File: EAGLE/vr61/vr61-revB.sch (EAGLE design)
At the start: 186 parts, among them M1 M25C, X1 MICROMOD-2222-C

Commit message: minor edits
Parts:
- added S3: BOOT, SparkFun-Switches:MOMENTARY-SWITCH-SPST-SMD-5.2-TALL-REDUNDANT
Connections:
- net !BOOT: now also S3.2
- net GND: now also S3.1
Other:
- note added: "Do not populate"
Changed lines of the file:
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@@
 <part name="J-52" library="SparkFun-Connectors" library_urn="urn:adsk.eagle:library:513" deviceset="CONN_03" device="" package3d_urn="urn:adsk.eagle:package:38063/1"/>
 <part name="U$14" library="ts_keyboards" deviceset="74AHCT1G125GW" device=""/>
+<part name="S3" library="SparkFun-Switches" deviceset="MOMENTARY-SWITCH-SPST" device="-SMD-5.2-TALL-REDUNDANT" value="BOOT"/>
 </parts>
 <sheets>
@@
 <text x="48.26" y="58.42" size="1.778" layer="91">SPI EEPROM</text>
 <text x="180.34" y="55.88" size="1.778" layer="91">TE P# 2199119-4</text>
+<text x="269.24" y="157.48" size="1.778" layer="91" rot="R90">Do not populate</text>
+<text x="67.818" y="37.084" size="1.778" layer="91" rot="R180">Do not populate</text>
 </plain>
 <instances>
@@
 <attribute name="NAME" x="256.54" y="162.052" size="1.778" layer="95" font="vector" rot="R180"/>
 </instance>
-<instance part="GND10" gate="1" x="243.84" y="162.56" smashed="yes">
-<attribute name="VALUE" x="243.84" y="157.988" size="1.778" layer="96" align="top-center"/>
+<instance part="GND10" gate="1" x="241.3" y="157.48" smashed="yes">
+<attribute name="VALUE" x="241.3" y="152.908" size="1.778" layer="96" align="top-center"/>
 </instance>
 <instance part="U$4" gate="G$1" x="248.92" y="63.5" smashed="yes">
@@
 <attribute name="NAME" x="147.32" y="21.59" size="1.27" layer="95"/>
 <attribute name="VALUE" x="143.256" y="8.128" size="1.27" layer="96"/>
+</instance>
+<instance part="S3" gate="G$1" x="264.16" y="165.1" smashed="yes" rot="R90">
+<attribute name="NAME" x="262.636" y="165.1" size="1.778" layer="95" font="vector" rot="R90" align="bottom-center"/>
+<attribute name="VALUE" x="264.668" y="165.1" size="1.778" layer="96" font="vector" rot="R90" align="top-center"/>
 </instance>
 </instances>
@@
 <wire x1="246.38" y1="165.1" x2="243.84" y2="165.1" width="0.1524" layer="91"/>
 <pinref part="GND10" gate="1" pin="GND"/>
-<wire x1="243.84" y1="165.1" x2="243.84" y2="162.56" width="0.1524" layer="91"/>
+<wire x1="243.84" y1="165.1" x2="241.3" y2="165.1" width="0.1524" layer="91"/>
+<wire x1="241.3" y1="165.1" x2="241.3" y2="157.48" width="0.1524" layer="91"/>
+<pinref part="S3" gate="G$1" pin="1"/>
+<wire x1="264.16" y1="160.02" x2="264.16" y2="157.48" width="0.1524" layer="91"/>
+<wire x1="264.16" y1="157.48" x2="246.38" y2="157.48" width="0.1524" layer="91"/>
+<wire x1="246.38" y1="157.48" x2="246.38" y2="160.02" width="0.1524" layer="91"/>
+<wire x1="246.38" y1="160.02" x2="243.84" y2="160.02" width="0.1524" layer="91"/>
+<wire x1="243.84" y1="160.02" x2="243.84" y2="165.1" width="0.1524" layer="91"/>
+<junction x="243.84" y="165.1"/>
 </segment>
 <segment>
@@
 <pinref part="J-BOOT" gate="G$1" pin="1"/>
 <wire x1="246.38" y1="167.64" x2="243.84" y2="167.64" width="0.1524" layer="91"/>
-<label x="243.84" y="167.64" size="1.778" layer="95" rot="R180" xref="yes"/>
-</segment>
-</net>
+<label x="241.3" y="167.64" size="1.778" layer="95" rot="R180" xref="yes"/>
+<wire x1="243.84" y1="167.64" x2="241.3" y2="167.64" width="0.1524" layer="91"/>
+<wire x1="243.84" y1="167.64" x2="243.84" y2="172.72" width="0.1524" layer="91"/>
+<junction x="243.84" y="167.64"/>
+<wire x1="243.84" y1="172.72" x2="264.16" y2="172.72" width="0.1524" layer="91"/>
+<pinref part="S3" gate="G$1" pin="2"/>
+<wire x1="264.16" y1="172.72" x2="264.16" y2="170.18" width="0.1524" layer="91"/>
+</segment>
+</net>

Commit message: Reb B.2 update
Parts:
- removed JP-VIN3: OPT, SparkFun-Jumpers:JUMPER-SMT_2_NC_PASTE_NO-SILK
- added D63, D64, D65, D66, D67: (no value), jlcpcb_basic_parts:1N5819WS
- added DIP-SW: DIP004, untitled:DIP004
- added J-VIN: (no value), ts_jumpers:JUMPER-1X2
- added S_BSPC2, S_CAPS2, S_FN, S_RSFT2, S_SPARE: MX-5-PIN-MILMAX-3305-XNO-SILK, ts_keyboards:MX-5-PIN-MILMAX-3305-XNO-SILK
- added U$20, U$21, U$22: FIDUCIAL, __temp_to_delete:FIDUCIAL
- JP-GND: device SparkFun-Jumpers:JUMPER-SMT_2_NO_NO-SILK -> ts_jumpers:JUMPER-1X2
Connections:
- removed net N$68: JP-VIN3.1, R3.2
- new net N$70: D64.A, S_SPARE.P
- new net N$71: D63.A, S_FN.P
- new net N$73: D65.A, DIP-SW.1
- new net N$74: DIP-SW.4, J-VIN.2, R3.2
- new net N$75: D66.A, DIP-SW.2
- new net N$76: D67.A, DIP-SW.3
- net GROUND: now also JP-GND.2; no longer JP-GND.1
- net MX4: now also D63.C, D64.C
- net MX5: now also D65.C, D66.C, D67.C
- net MY2: now also S_CAPS2.P
- net MY5: now also DIP-SW.8, S_BSPC2.S
- net MY6: now also DIP-SW.7
- net MY7: now also DIP-SW.6, S_SPARE.S
- net MY8: now also S_FN.S, S_RSFT2.S
- net N$14: now also S_BSPC2.P
- net N$53: now also S_RSFT2.P
- net N$62: now also S_CAPS2.S
- net SC1: now also JP-GND.1; no longer JP-GND.2
- net VSUP: now also DIP-SW.5, J-VIN.1; no longer JP-VIN3.2
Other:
- note added: "<<< DNP >>> (Do Not Populate)"
- note added: "OPTIONAL Micromod Voltage Sensor & DIP Switches <<< DNP >>>"
- note removed: "Micromod Voltage Sensor"
- moved on the sheet: D01, D02, D03, D04, D05, D06, D07, D08, D09, D10, D11, D12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

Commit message: Boot switch redo
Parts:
- added C14: 100nF, rcl:C-EUC0603
- added D80: BAS70-05, diode:BAS70-05
- added R9: 5.1K, rcl:R-EU_R0603
- added S4: BOOT, SparkFun-Switches:MOMENTARY-SWITCH-SPST-SMD-5.2-TALL-REDUNDANT
- S1: value Reset -> (none); device SparkFun-Switches:MOMENTARY-SWITCH-SPST-SMD-5.2-TALL-REDUNDANT -> VinoRodrigues_Custom_Eagle:MOMENTARY-SWITCH-SPST-1
- S2: value BOOT -> (none); device SparkFun-Switches:MOMENTARY-SWITCH-SPST-SMD-5.2-TALL-REDUNDANT -> VinoRodrigues_Custom_Eagle:MOMENTARY-SWITCH-SPST-1
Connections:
- new net BOOT: D80.C, J-BOOT.1, R9.1, S3.2, S4.2
- net !BOOT: now also C14.1, D80.A1, S2.3; no longer J-BOOT.1, S2.2, S3.2
- net !RESET: now also D80.A2, S1.3; no longer S1.2
- net GND: now also C14.2, S4.1
- net VCC: now also R9.2
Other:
- note added: "<<< DNP >>> (Do Not Populate) for under space bar"
- note removed: "<<< DNP >>> (Do Not Populate)"
- moved on the sheet: S3

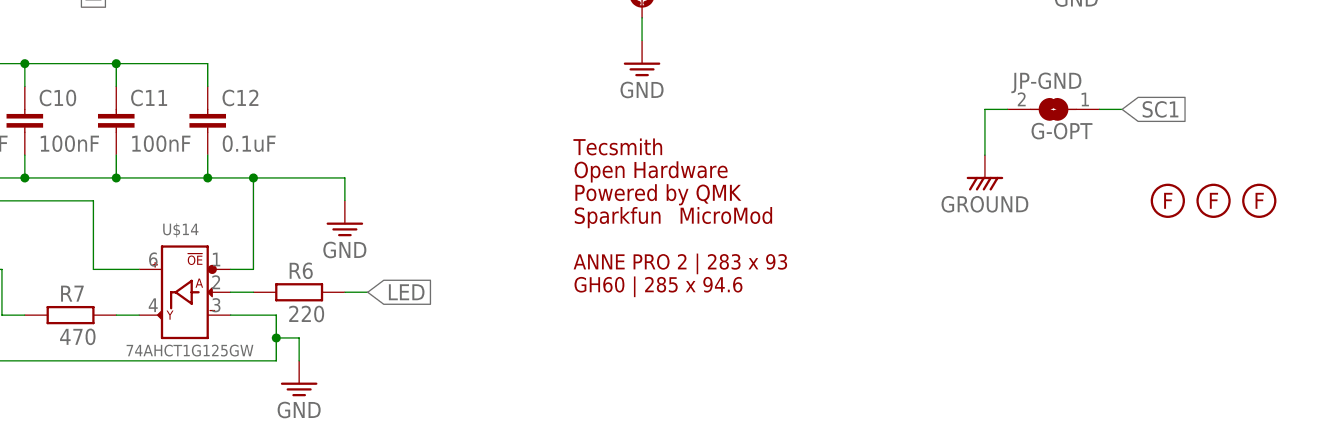
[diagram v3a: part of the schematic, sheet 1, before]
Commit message: Added Bakeneko footprint
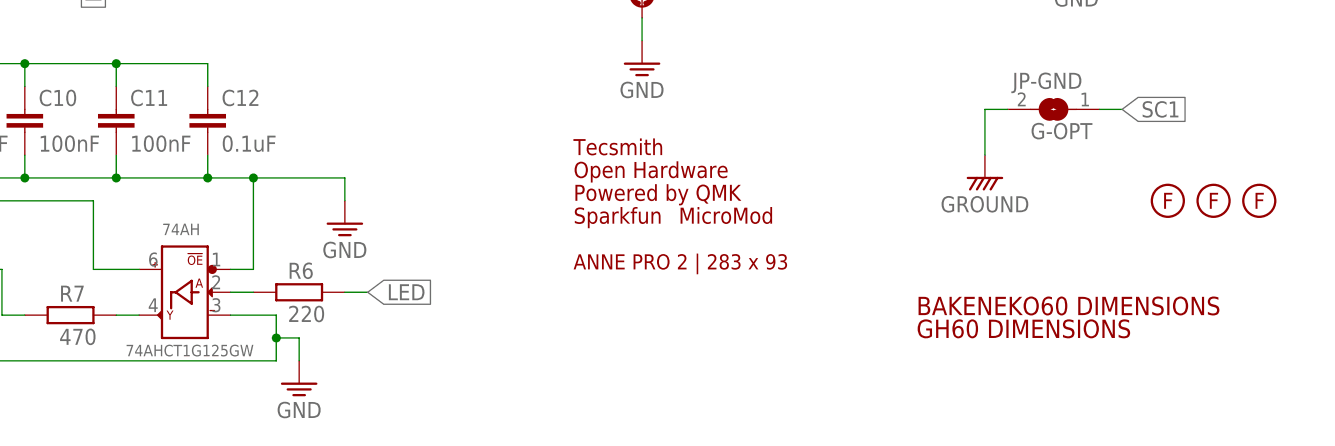
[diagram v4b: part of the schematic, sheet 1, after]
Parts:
- removed FP_GH60: FOOTPRINT-GH60, ts_keyboards:FOOTPRINT-GH60
- added U$24: FOOTPRINT-BAKENEKO60, ts_keyboards:FOOTPRINT-BAKENEKO60
- added U$25: FOOTPRINT-DIMS-GH60, ts_keyboards:FOOTPRINT-DIMS-GH60
- renumbered U$14 to 74AH
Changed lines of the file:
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@@
 <part name="GND13" library="ts_custom_nick_nacks" deviceset="GND" device=""/>
 <part name="FP_AP2" library="ts_keyboards" deviceset="FOOTPRINT-AP2" device=""/>
-<part name="FP_GH60" library="ts_keyboards" deviceset="FOOTPRINT-GH60" device=""/>
 <part name="D43" library="jlcpcb_basic_parts" deviceset="1N5819WS" device=""/>
 <part name="S_NUBS" library="ts_keyboards" deviceset="MX-5-PIN-HOTSWAP-PAD" device="NO-SILK"/>
@@
 <part name="T_ENT1" library="ts_keyboards" deviceset="MX-STABS-200U" device=""/>
 <part name="J-52" library="SparkFun-Connectors" library_urn="urn:adsk.eagle:library:513" deviceset="CONN_03" device="" package3d_urn="urn:adsk.eagle:package:38063/1"/>
-<part name="U$14" library="ts_keyboards" deviceset="74AHCT1G125GW" device=""/>
+<part name="74AH" library="ts_keyboards" deviceset="74AHCT1G125GW" device=""/>
 <part name="S4" library="SparkFun-Switches" deviceset="MOMENTARY-SWITCH-SPST" device="-SMD-5.2-TALL-REDUNDANT" value="BOOT"/>
 <part name="D63" library="jlcpcb_basic_parts" deviceset="1N5819WS" device=""/>
@@
 <part name="U$23" library="ts_custom_nick_nacks" deviceset="3V3" device=""/>
 <part name="GND14" library="ts_custom_nick_nacks" deviceset="GND" device=""/>
+<part name="U$24" library="ts_keyboards" deviceset="FOOTPRINT-BAKENEKO60" device=""/>
+<part name="U$25" library="ts_keyboards" deviceset="FOOTPRINT-DIMS-GH60" device=""/>
 </parts>
 <sheets>
@@
 </instance>
 <instance part="FP_AP2" gate="G$1" x="193.04" y="17.78" smashed="yes"/>
-<instance part="FP_GH60" gate="G$1" x="193.04" y="15.24" smashed="yes"/>
 <instance part="J-HOST" gate="G$1" x="160.02" y="124.46" smashed="yes">
 <attribute name="VALUE" x="157.48" y="119.634" size="1.778" layer="96" font="vector"/>
@@
 <attribute name="NAME" x="236.22" y="64.008" size="1.778" layer="95" font="vector"/>
 </instance>
-<instance part="U$14" gate="G$1" x="149.86" y="15.24" smashed="yes">
+<instance part="74AH" gate="G$1" x="149.86" y="15.24" smashed="yes">
 <attribute name="NAME" x="147.32" y="21.59" size="1.27" layer="95"/>
 <attribute name="VALUE" x="143.256" y="8.128" size="1.27" layer="96"/>
@@
 <attribute name="VALUE" x="124.46" y="51.308" size="1.778" layer="96" align="top-center"/>
 </instance>
+<instance part="U$24" gate="G$1" x="231.14" y="12.7" smashed="yes"/>
+<instance part="U$25" gate="G$1" x="231.14" y="10.16" smashed="yes"/>
 </instances>
 <busses>
@@
 <wire x1="162.56" y1="10.16" x2="160.02" y2="10.16" width="0.1524" layer="91"/>
 <junction x="160.02" y="10.16"/>
-<pinref part="U$14" gate="G$1" pin="3_GND"/>
+<pinref part="74AH" gate="G$1" pin="3_GND"/>
 </segment>
 <segment>
@@
 <wire x1="157.48" y1="17.78" x2="157.48" y2="27.94" width="0.1524" layer="91"/>
 <junction x="157.48" y="27.94"/>
-<pinref part="U$14" gate="G$1" pin="!OE"/>
+<pinref part="74AH" gate="G$1" pin="!OE"/>
 <wire x1="157.48" y1="17.78" x2="154.94" y2="17.78" width="0.1524" layer="91"/>
 </segment>
@@
 <wire x1="96.52" y1="40.64" x2="96.52" y2="25.4" width="0.1524" layer="91"/>
 <junction x="96.52" y="25.4"/>
-<pinref part="U$14" gate="G$1" pin="5_VCC"/>
+<pinref part="74AH" gate="G$1" pin="5_VCC"/>
 </segment>
 </net>
@@
 <pinref part="R6" gate="G$1" pin="1"/>
 <wire x1="157.48" y1="15.24" x2="154.94" y2="15.24" width="0.1524" layer="91"/>
-<pinref part="U$14" gate="G$1" pin="A_DIN"/>
+<pinref part="74AH" gate="G$1" pin="A_DIN"/>
 </segment>
 </net>
@@
 <pinref part="R7" gate="G$1" pin="2"/>
 <wire x1="144.78" y1="12.7" x2="142.24" y2="12.7" width="0.1524" layer="91"/>
-<pinref part="U$14" gate="G$1" pin="Y_DOUT"/>
-</segment>
-</net>
+<pinref part="74AH" gate="G$1" pin="Y_DOUT"/>
+</segment>
+</net>

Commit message: .
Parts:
- added U$26: ?, tecsmith_jlcpcb_ordering:JLC_ORDER_NUMBER_QRQR_5X5
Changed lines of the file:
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@@
 <part name="U$24" library="ts_keyboards" deviceset="FOOTPRINT-BAKENEKO60" device=""/>
 <part name="U$25" library="ts_keyboards" deviceset="FOOTPRINT-DIMS-GH60" device=""/>
+<part name="U$26" library="tecsmith_jlcpcb_ordering" deviceset="JLC_ORDER_NUMBER_QR" device="QR_5X5" value="?"/>
 </parts>
 <sheets>
@@
 <attribute name="NAME" x="11.43" y="100.838" size="1.778" layer="95" rot="MR90"/>
 </instance>
+<instance part="U$26" gate="G$1" x="226.568" y="6.35" smashed="yes"/>
 </instances>
 <busses>
